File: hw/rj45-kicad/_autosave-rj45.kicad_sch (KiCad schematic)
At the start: 50 parts

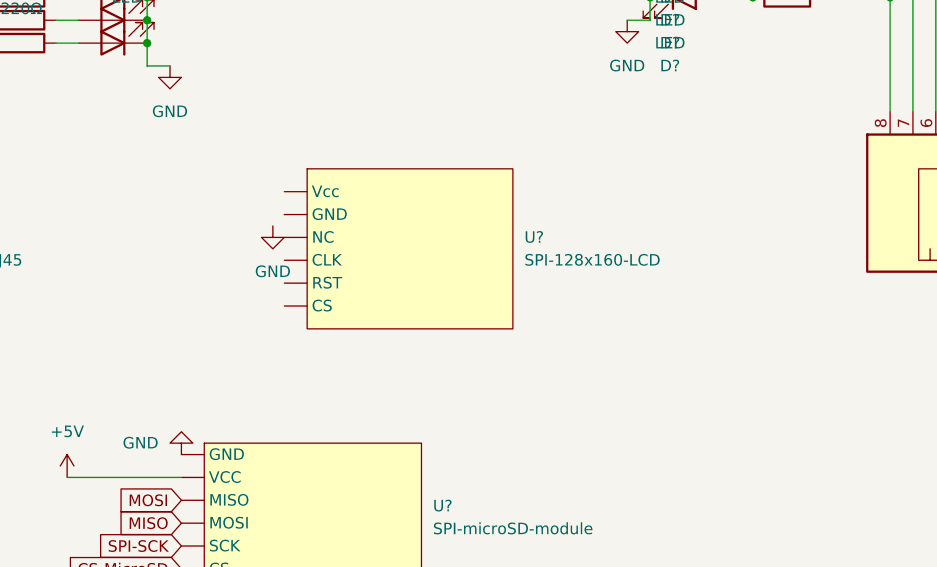
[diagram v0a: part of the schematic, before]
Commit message: Cannot switch cable mode while testing
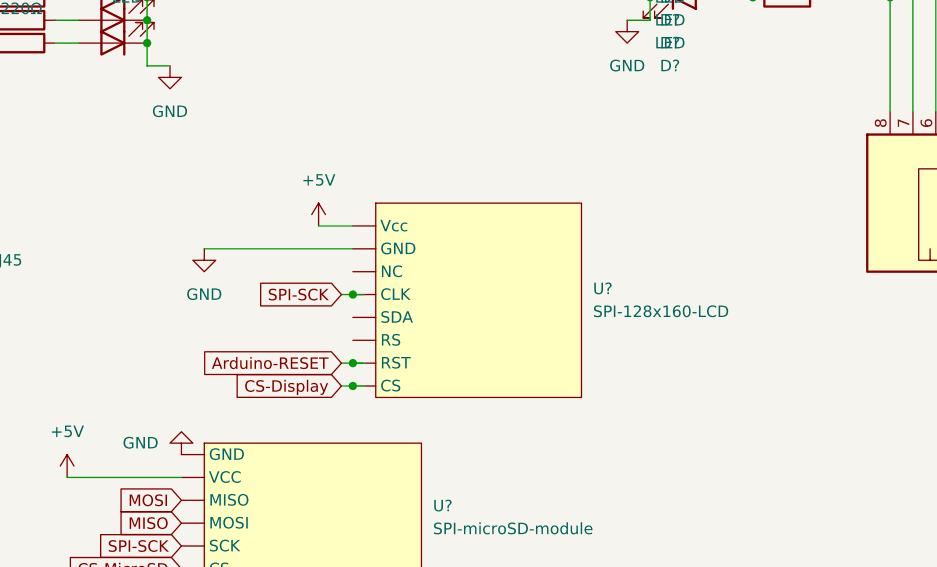
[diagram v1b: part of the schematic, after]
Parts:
- removed U?: SPI-128x160-LCD, symbol custom-parts:SPI-128x160-LCD
- added U?: SPI-128x160-LCD, symbol custom-parts:SPI-128x160-LCD
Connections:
- net +5V: now also U?. (Vcc)
- net CS-Display: now also U?. (Vcc)
- net GND: now also U?. (Vcc)
- net SPI-SCK: now also U?. (Vcc)
- new net Arduino-RESET: U?. (Vcc)
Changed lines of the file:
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@@
   (junction (at 118.11 86.36) (diameter 0) (color 0 0 0 0)
   )
+  (junction (at 140.97 132.08) (diameter 0) (color 0 0 0 0)
+  )
   (junction (at 86.36 86.36) (diameter 0) (color 0 0 0 0)
   )
@@
   (junction (at 173.99 78.74) (diameter 0) (color 0 0 0 0)
   )
+  (junction (at 140.97 129.54) (diameter 0) (color 0 0 0 0)
+  )
   (junction (at 91.44 81.28) (diameter 0) (color 0 0 0 0)
   )
@@
   (junction (at 78.74 93.98) (diameter 0) (color 0 0 0 0)
   )
+  (junction (at 140.97 121.92) (diameter 0) (color 0 0 0 0)
+  )
   (junction (at 50.8 171.45) (diameter 0) (color 0 0 0 0)
   )
@@
     (stroke (width 0) (type default) (color 0 0 0 0))
   )
+  (wire (pts (xy 140.97 132.08) (xy 142.24 132.08))
+    (stroke (width 0) (type default) (color 0 0 0 0))
+  )
   (wire (pts (xy 124.46 162.56) (xy 127 162.56))
     (stroke (width 0) (type default) (color 0 0 0 0))
@@
     (stroke (width 0) (type default) (color 0 0 0 0))
   )
+  (wire (pts (xy 140.97 129.54) (xy 142.24 129.54))
+    (stroke (width 0) (type default) (color 0 0 0 0))
+  )
   (wire (pts (xy 236.22 76.2) (xy 213.36 76.2))
     (stroke (width 0) (type default) (color 0 0 0 0))
@@
     (stroke (width 0) (type default) (color 0 0 0 0))
   )
+  (wire (pts (xy 139.7 121.92) (xy 140.97 121.92))
+    (stroke (width 0) (type default) (color 0 0 0 0))
+  )
   (wire (pts (xy 185.42 86.36) (xy 186.69 86.36))
     (stroke (width 0) (type default) (color 0 0 0 0))
   )
+  (wire (pts (xy 140.97 121.92) (xy 142.24 121.92))
+    (stroke (width 0) (type default) (color 0 0 0 0))
+  )
   (wire (pts (xy 71.12 78.74) (xy 93.98 78.74))
     (stroke (width 0) (type default) (color 0 0 0 0))
@@
     (stroke (width 0) (type default) (color 0 0 0 0))
   )
+  (wire (pts (xy 137.16 114.3) (xy 140.97 114.3))
+    (stroke (width 0) (type default) (color 0 0 0 0))
+  )
   (wire (pts (xy 173.99 73.66) (xy 173.99 76.2))
     (stroke (width 0) (type default) (color 0 0 0 0))
@@
     (stroke (width 0) (type default) (color 0 0 0 0))
   )
+  (wire (pts (xy 139.7 129.54) (xy 140.97 129.54))
+    (stroke (width 0) (type default) (color 0 0 0 0))
+  )
   (wire (pts (xy 78.74 172.72) (xy 78.74 171.45))
     (stroke (width 0) (type default) (color 0 0 0 0))
@@
   )
   (wire (pts (xy 50.8 167.64) (xy 58.42 167.64))
+    (stroke (width 0) (type default) (color 0 0 0 0))
+  )
+  (wire (pts (xy 124.46 116.84) (xy 140.97 116.84))
+    (stroke (width 0) (type default) (color 0 0 0 0))
+  )
+  (wire (pts (xy 139.7 132.08) (xy 140.97 132.08))
     (stroke (width 0) (type default) (color 0 0 0 0))
   )
@@
     )
   )
+  (global_label "SPI-SCK" (shape input) (at 139.7 121.92 180) (fields_autoplaced)
+    (effects (font (size 1.27 1.27)) (justify right))
+    (property "Intersheet References" "${INTERSHEET_REFS}" (id 0) (at 128.8807 121.8406 0)
+      (effects (font (size 1.27 1.27)) (justify right) hide)
+    )
+  )
   (global_label "MISO" (shape input) (at 129.54 60.96 180) (fields_autoplaced)
     (effects (font (size 1.27 1.27)) (justify right))
@@
     )
   )
+  (global_label "Arduino-RESET" (shape input) (at 139.7 129.54 180) (fields_autoplaced)
+    (effects (font (size 1.27 1.27)) (justify right))
+    (property "Intersheet References" "${INTERSHEET_REFS}" (id 0) (at 122.8936 129.4606 0)
+      (effects (font (size 1.27 1.27)) (justify right) hide)
+    )
+  )
   (global_label "74HC165-DATA-IN" (shape input) (at 261.62 68.58 0) (fields_autoplaced)
     (effects (font (size 1.27 1.27)) (justify left))
@@
     )
   )
+  (global_label "CS-Display" (shape input) (at 139.7 132.08 180) (fields_autoplaced)
+    (effects (font (size 1.27 1.27)) (justify right))
+    (property "Intersheet References" "${INTERSHEET_REFS}" (id 0) (at 126.4012 132.0006 0)
+      (effects (font (size 1.27 1.27)) (justify right) hide)
+    )
+  )
   (global_label "74HC595-DATA-OUT" (shape input) (at 35.56 83.82 180) (fields_autoplaced)
     (effects (font (size 1.27 1.27)) (justify right))
@@
     (pin "1")
     (pin "2")
+  )
+  (symbol (lib_id "custom-parts:SPI-128x160-LCD") (at 154.94 124.46 0) (unit 1)
+    (in_bom yes) (on_board yes) (fields_autoplaced)
+    (property "Reference" "U?" (id 0) (at 167.64 121.2849 0)
+      (effects (font (size 1.27 1.27)) (justify left))
+    )
+    (property "Value" "SPI-128x160-LCD" (id 1) (at 167.64 123.8249 0)
+      (effects (font (size 1.27 1.27)) (justify left))
+    )
+    (property "Footprint" "" (id 2) (at 154.94 110.49 0)
+      (effects (font (size 1.27 1.27)) hide)
+    )
+    (property "Datasheet" "" (id 3) (at 154.94 110.49 0)
+      (effects (font (size 1.27 1.27)) hide)
+    )
+    (pin "")
+    (pin "")
+    (pin "")
+    (pin "")
+    (pin "")
+    (pin "")
+    (pin "")
+    (pin "")
   )
   (symbol (lib_id "power:GND") (at 142.24 73.66 0) (unit 1)
@@
     (pin "2")
   )
-  (symbol (lib_id "custom-parts:SPI-128x160-LCD") (at 147.32 116.84 0) (unit 1)
-    (in_bom yes) (on_board yes) (fields_autoplaced)
-    (property "Reference" "U?" (id 0) (at 160.02 115.5699 0)
-      (effects (font (size 1.27 1.27)) (justify left))
-    )
-    (property "Value" "SPI-128x160-LCD" (id 1) (at 160.02 118.1099 0)
-      (effects (font (size 1.27 1.27)) (justify left))
-    )
-    (property "Footprint" "" (id 2) (at 147.32 106.68 0)
-      (effects (font (size 1.27 1.27)) hide)
-    )
-    (property "Datasheet" "" (id 3) (at 147.32 106.68 0)
-      (effects (font (size 1.27 1.27)) hide)
-    )
-    (pin "")
-    (pin "")
-    (pin "")
-    (pin "")
-    (pin "")
-    (pin "")
-  )
   (symbol (lib_id "power:+5V") (at 109.22 142.24 0) (unit 1)
     (in_bom yes) (on_board yes) (fields_autoplaced)
@@
     (pin "2")
   )
+  (symbol (lib_id "power:+5V") (at 137.16 114.3 0) (unit 1)
+    (in_bom yes) (on_board yes) (fields_autoplaced)
+    (property "Reference" "#PWR?" (id 0) (at 137.16 118.11 0)
+      (effects (font (size 1.27 1.27)) hide)
+    )
+    (property "Value" "+5V" (id 1) (at 137.16 109.22 0))
+    (property "Footprint" "" (id 2) (at 137.16 114.3 0)
+      (effects (font (size 1.27 1.27)) hide)
+    )
+    (property "Datasheet" "" (id 3) (at 137.16 114.3 0)
+      (effects (font (size 1.27 1.27)) hide)
+    )
+    (pin "1")
+  )
   (symbol (lib_id "power:+5V") (at 124.46 162.56 0) (unit 1)
     (in_bom yes) (on_board yes) (fields_autoplaced)
@@
     (pin "2")
   )
-  (symbol (lib_id "power:GND") (at 132.08 114.3 0) (unit 1)
-    (in_bom yes) (on_board yes) (fields_autoplaced)
-    (property "Reference" "#PWR?" (id 0) (at 132.08 120.65 0)
-      (effects (font (size 1.27 1.27)) hide)
-    )
-    (property "Value" "GND" (id 1) (at 132.08 119.38 0))
-    (property "Footprint" "" (id 2) (at 132.08 114.3 0)
-      (effects (font (size 1.27 1.27)) hide)
-    )
-    (property "Datasheet" "" (id 3) (at 132.08 114.3 0)
+  (symbol (lib_id "power:GND") (at 124.46 116.84 0) (unit 1)
+    (in_bom yes) (on_board yes) (fields_autoplaced)
+    (property "Reference" "#PWR?" (id 0) (at 124.46 123.19 0)
+      (effects (font (size 1.27 1.27)) hide)
+    )
+    (property "Value" "GND" (id 1) (at 124.46 121.92 0))
+    (property "Footprint" "" (id 2) (at 124.46 116.84 0)
+      (effects (font (size 1.27 1.27)) hide)
+    )
+    (property "Datasheet" "" (id 3) (at 124.46 116.84 0)
       (effects (font (size 1.27 1.27)) hide)
     )
@@
       (reference "#PWR?") (unit 1) (value "GND") (footprint "")
     )
+    (path "/9714d957-8b9f-41d4-b540-8bcd82462358"
+      (reference "#PWR?") (unit 1) (value "+5V") (footprint "")
+    )
     (path "/a3fece72-d7c7-49f7-b438-fec6b3a7273f"
       (reference "#PWR?") (unit 1) (value "+5V") (footprint "")
@@
       (reference "SW?") (unit 1) (value "SW_Push") (footprint "")
     )
-    (path "/4431aa31-d5b2-4ce8-b31f-e6a5057aaccb"
+    (path "/0b0ab2f9-b525-4231-aa59-2c1b00598b07"
       (reference "U?") (unit 1) (value "SPI-128x160-LCD") (footprint "")
     )
